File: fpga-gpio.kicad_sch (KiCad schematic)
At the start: 1 part, among them U1 MPFS250T-FCVG484

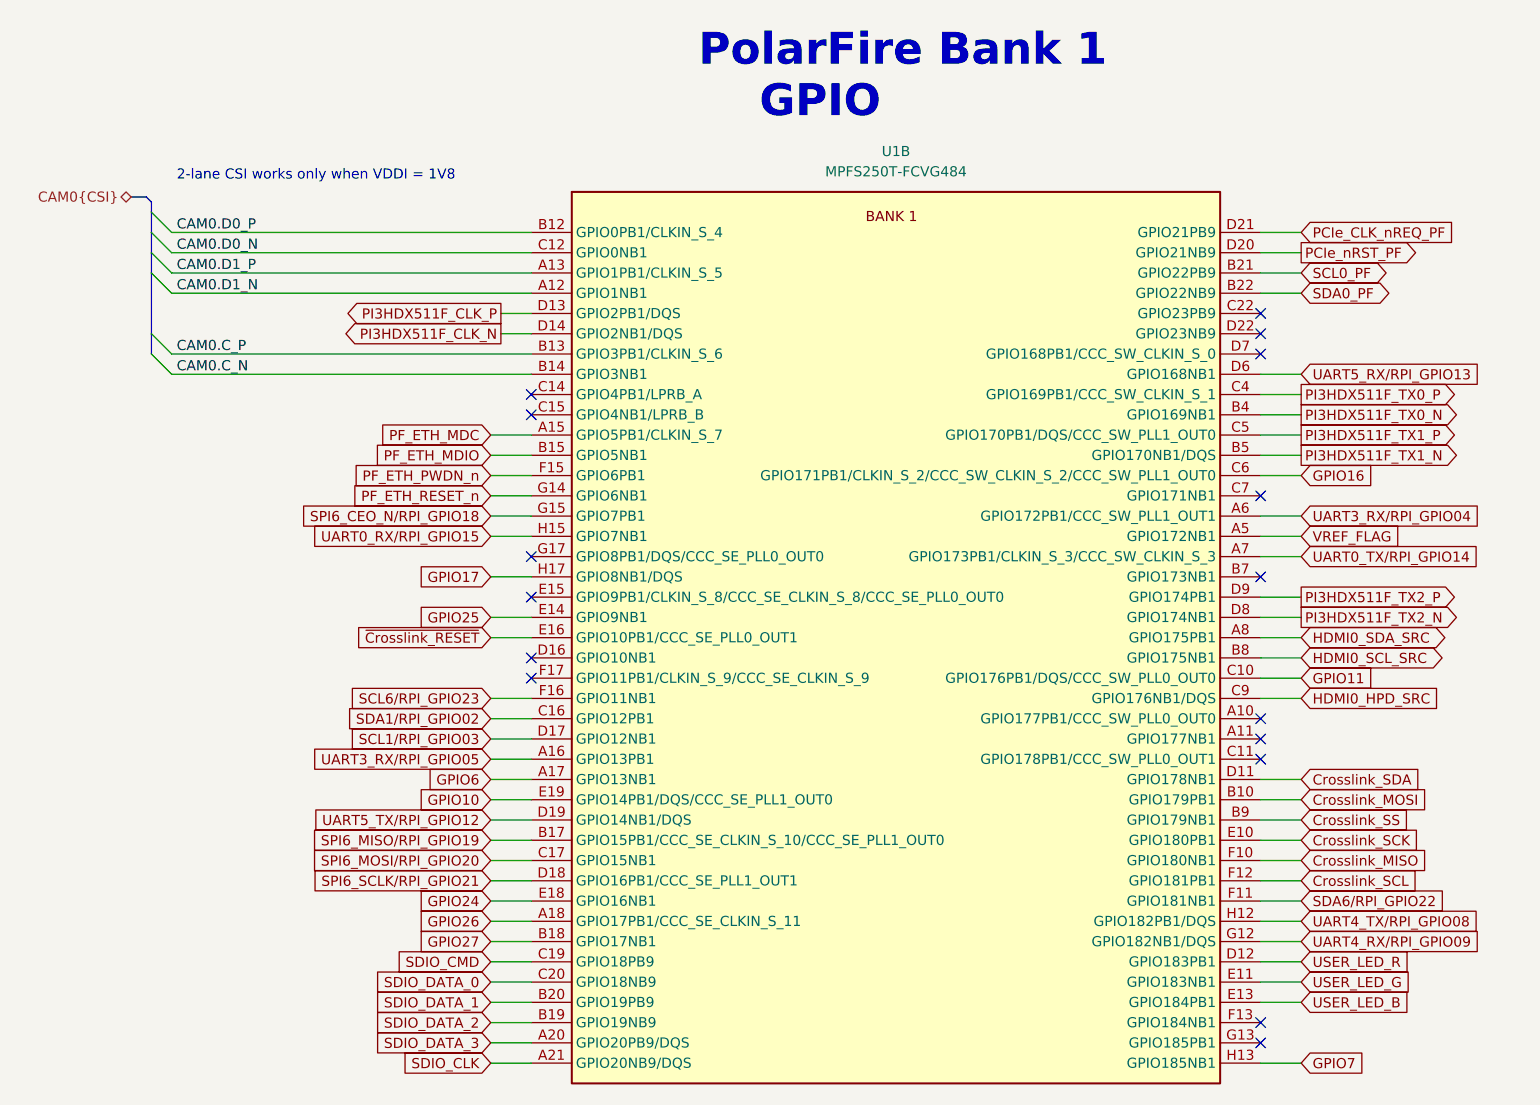
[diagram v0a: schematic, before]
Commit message: [#57505] Simplify config of WL_BT module, add level shifters
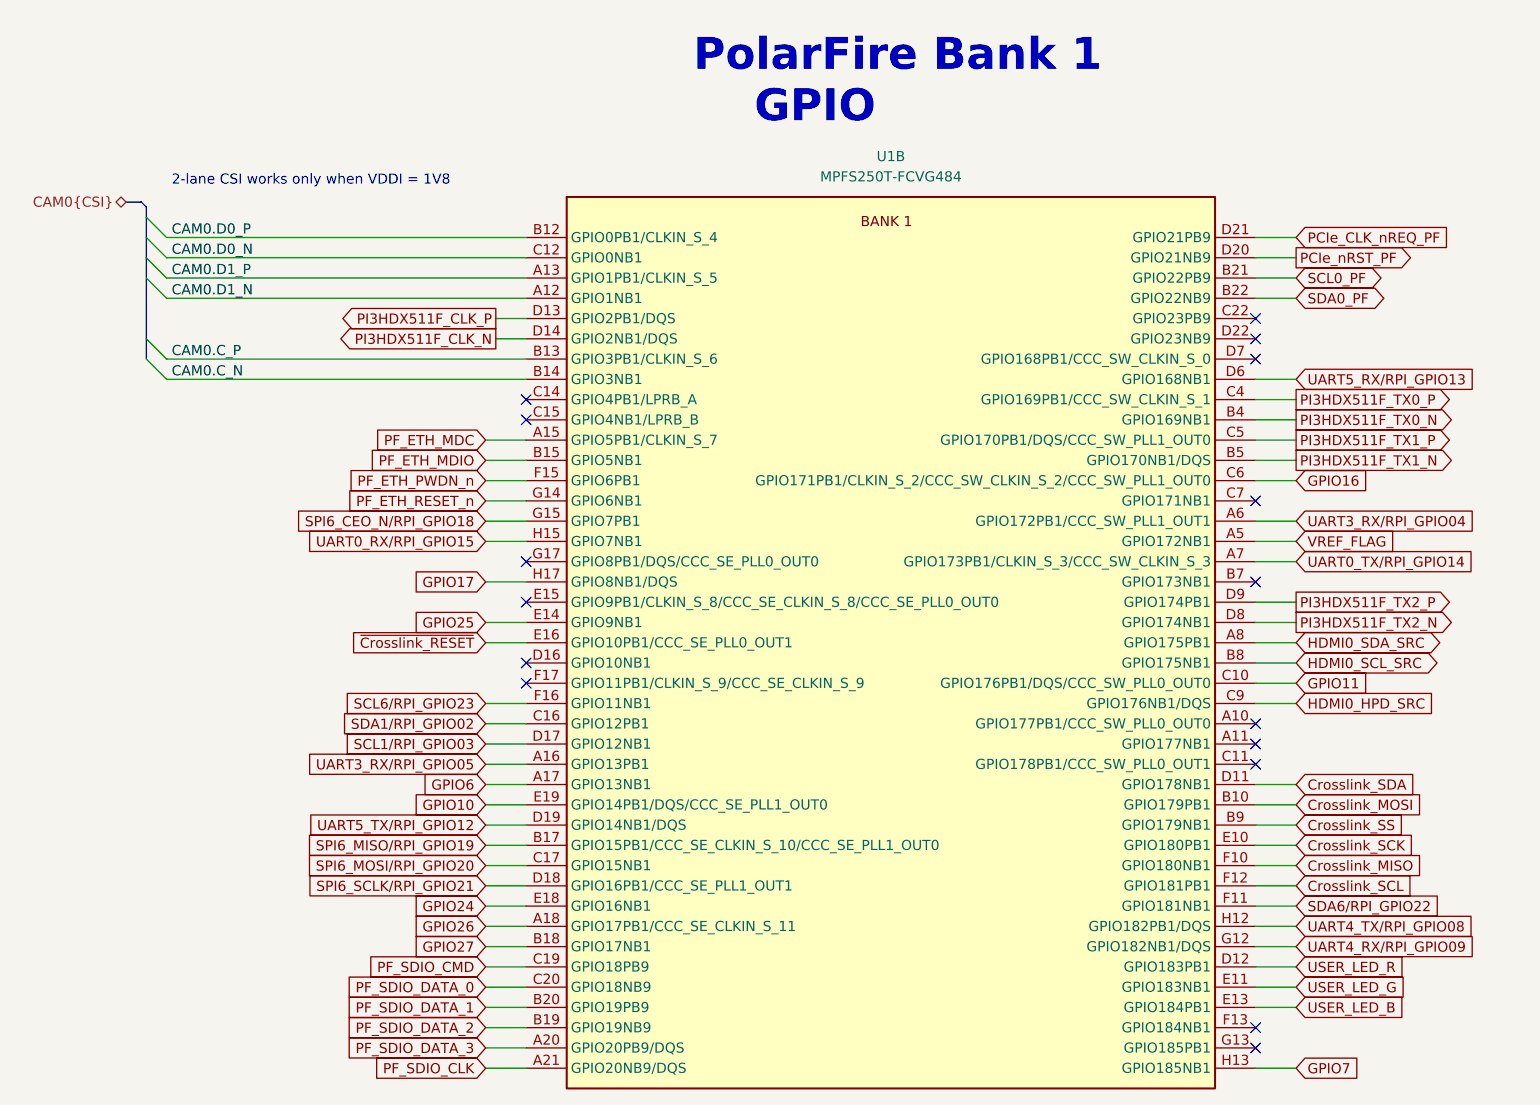
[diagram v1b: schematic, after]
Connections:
- net SDIO_CLK renamed PF_SDIO_CLK
- net SDIO_CMD renamed PF_SDIO_CMD
- net SDIO_DATA_0 renamed PF_SDIO_DATA_0
- net SDIO_DATA_1 renamed PF_SDIO_DATA_1
- net SDIO_DATA_2 renamed PF_SDIO_DATA_2
- net SDIO_DATA_3 renamed PF_SDIO_DATA_3
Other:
- moved on the sheet: U1B

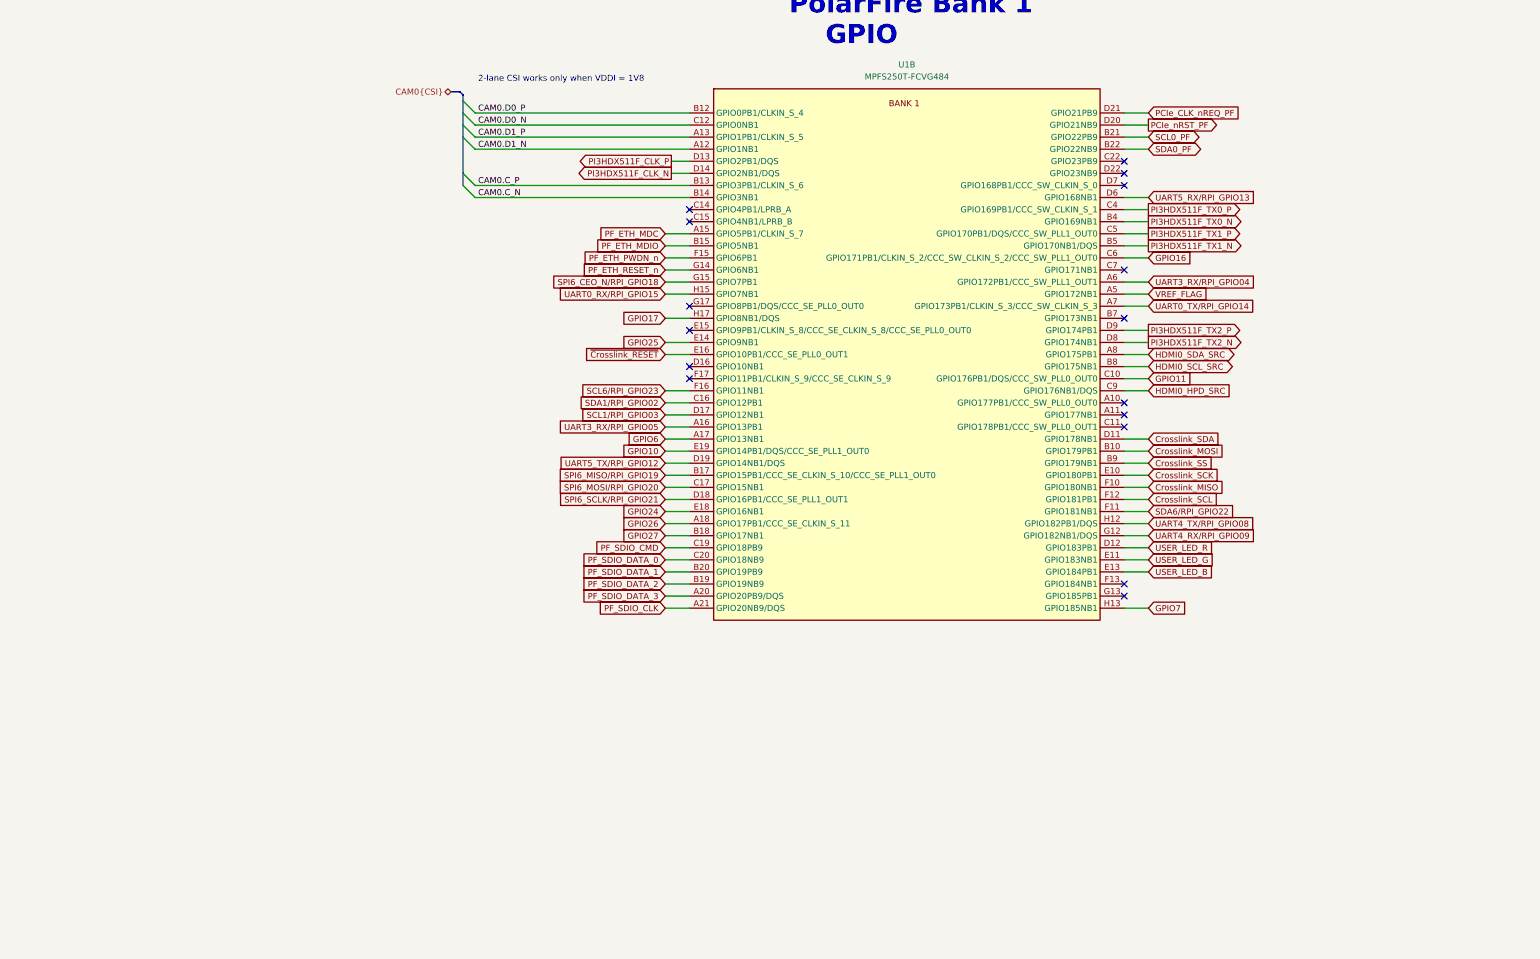
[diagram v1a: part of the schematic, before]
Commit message: [#57505] Continue migration to hierarchical schematic
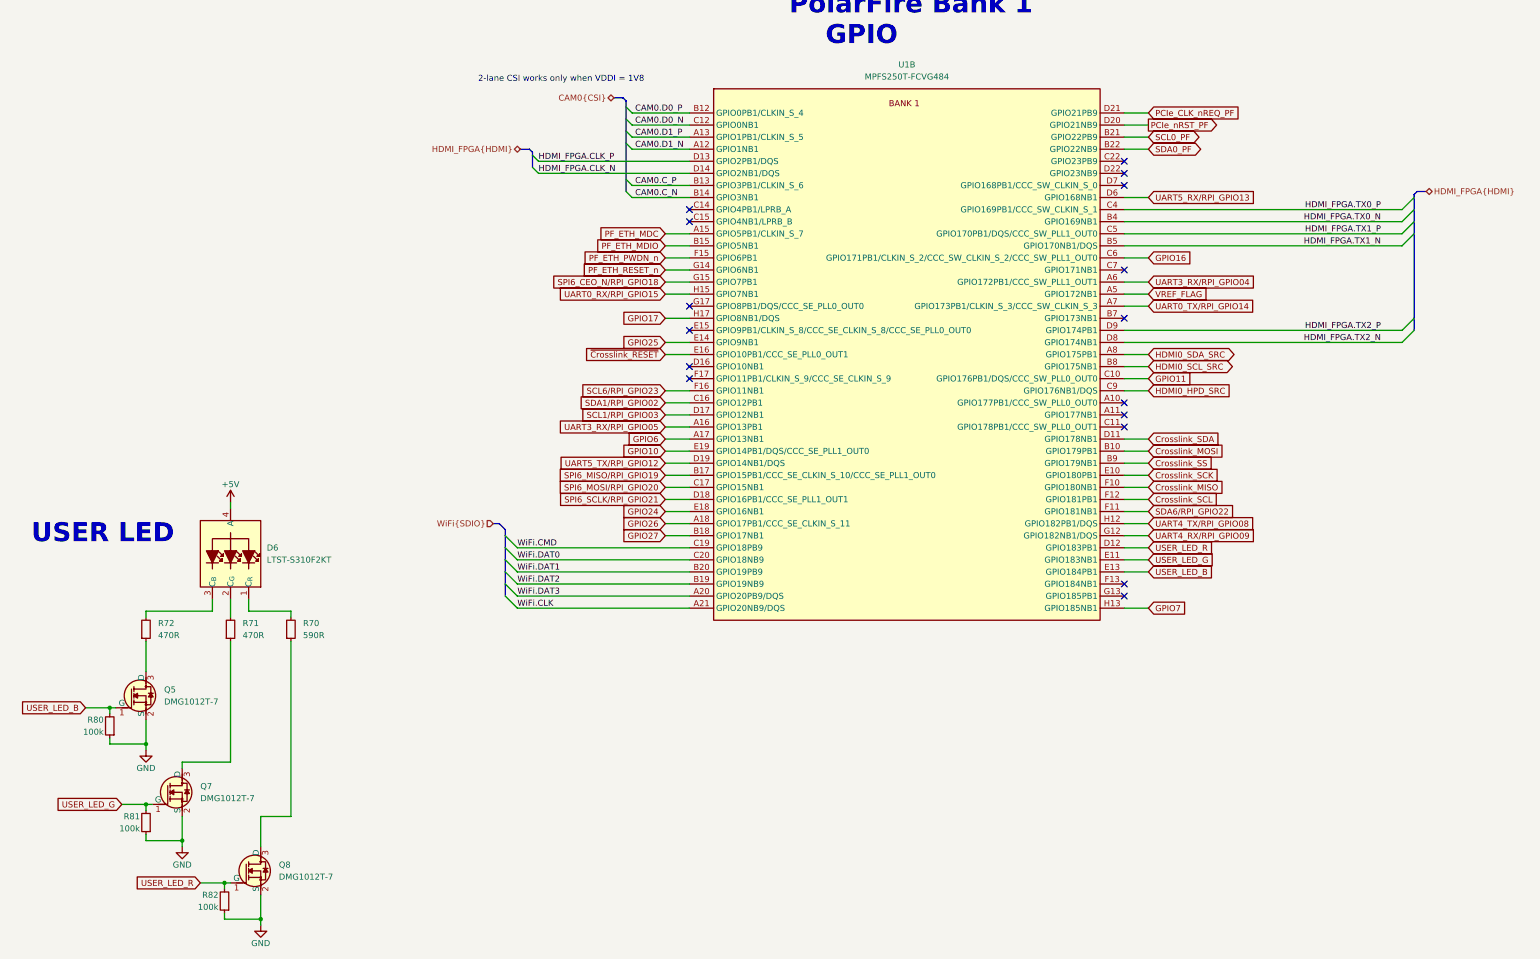
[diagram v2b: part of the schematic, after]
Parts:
- added D6: LED_RGB_1204_LTST-S310F2KT_Horizontal, antmicro-footprints:LED_1204_3210Metric_RGB, symbol antmicroLEDIndicationDiscrete:LED_RGB_1204_LTST-S310F2KT_Horizontal
- added Q5, Q7, Q8: DMG1012T-7, antmicro-footprints:SOT-523, symbol antmicroTransistorsFETsMOSFETsSingle:DMG1012T-7
- added R70: R_590R_0402, antmicro-footprints:R_0402_1005Metric, symbol antmicroResistors0402:R_590R_0402
- added R71, R72: R_470R_0402, antmicro-footprints:R_0402_1005Metric, symbol antmicroResistors0402:R_470R_0402
- added R80, R81, R82: R_100k_0402, antmicro-footprints:R_0402_1005Metric, symbol antmicroResistors0402:R_100k_0402
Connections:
- net USER_LED_B: now also Q5.1 (G), R80.2
- net USER_LED_G: now also Q7.1 (G), R81.2
- net USER_LED_R: now also Q8.1 (G), R82.2
- net PF_SDIO_CLK renamed WiFi.CLK
- net PF_SDIO_CMD renamed WiFi.CMD
- net PF_SDIO_DATA_0 renamed WiFi.DAT0
- net PF_SDIO_DATA_1 renamed WiFi.DAT1
- net PF_SDIO_DATA_2 renamed WiFi.DAT2
- net PF_SDIO_DATA_3 renamed WiFi.DAT3
- net PI3HDX511F_CLK_N renamed HDMI_FPGA.CLK_N
- net PI3HDX511F_CLK_P renamed HDMI_FPGA.CLK_P
- net PI3HDX511F_TX0_N renamed HDMI_FPGA.TX0_N
- net PI3HDX511F_TX0_P renamed HDMI_FPGA.TX0_P
- net PI3HDX511F_TX1_N renamed HDMI_FPGA.TX1_N
- net PI3HDX511F_TX1_P renamed HDMI_FPGA.TX1_P
- net PI3HDX511F_TX2_N renamed HDMI_FPGA.TX2_N
- net PI3HDX511F_TX2_P renamed HDMI_FPGA.TX2_P
- new net: Q7.3 (D), R71.1
- new net: D6.2 (C_{G}), R71.2
- new net: D6.1 (C_{R}), R70.2
- new net: D6.3 (C_{B}), R72.2
- new net: Q5.3 (D), R72.1
- new net: Q8.3 (D), R70.1
- new net +5V: D6.4 (A)
- new net GND: Q5.2 (S), Q7.2 (S), Q8.2 (S), R80.1, R81.1, R82.1
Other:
- note added: "USER LED"
